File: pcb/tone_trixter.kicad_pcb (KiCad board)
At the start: 2 copper layers, 132 x 57 mm, 103 parts, among them J1 INA jack lead, J10 microSD DM3AT, J2 OUT jack lead, J3 DC 2.1mm lead, J4 Battery lead, J5 Enclosure bond, J6 OLED 1.3" 7-pin, J7 SW-L bypass, J8 INB jack lead, J9 SW-R tuner, SW1 PEC11R-4220F-S0024, U1 OPA1642AIDR, U2 OPA1642AIDR, U3 OPA1642AIDR, U4 Daisy Seed3

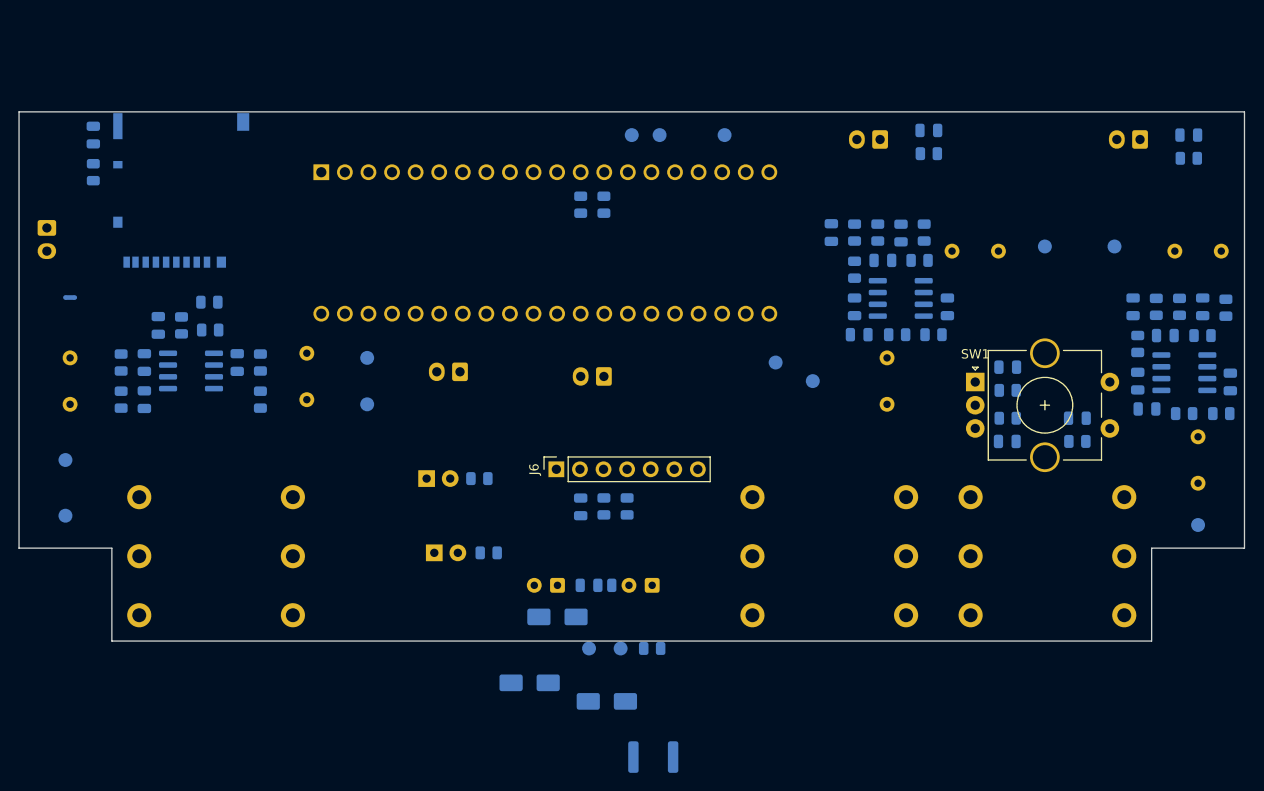
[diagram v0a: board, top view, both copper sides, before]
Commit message: pcb: output coupling caps to 1u C0G, LED/power/star placement pass
- gen_schematic: output C19/C21 10u film -> 1u C0G 1210 so they tuck
  under the OUT jack (C21->J2 tip run 3.0mm), matching the input caps
- LEDs D4/D5 forward to y=33.5 to clear the Daisy 2x20 pin field;
  silk alignment marks moved with them
- GND star (NT1) to the analog side, 6mm from the Daisy GNDA pin
- CH-B relaid under IN B (tip run 3.2mm); power section moved clear of
  the high-Z inputs (>=38mm) and out of the Daisy->USB corridor
- mirror_board_x.py: one-time X-mirror that set board handedness

Co-Authored-By: Claude Opus 4.8 <noreply@anthropic.com>
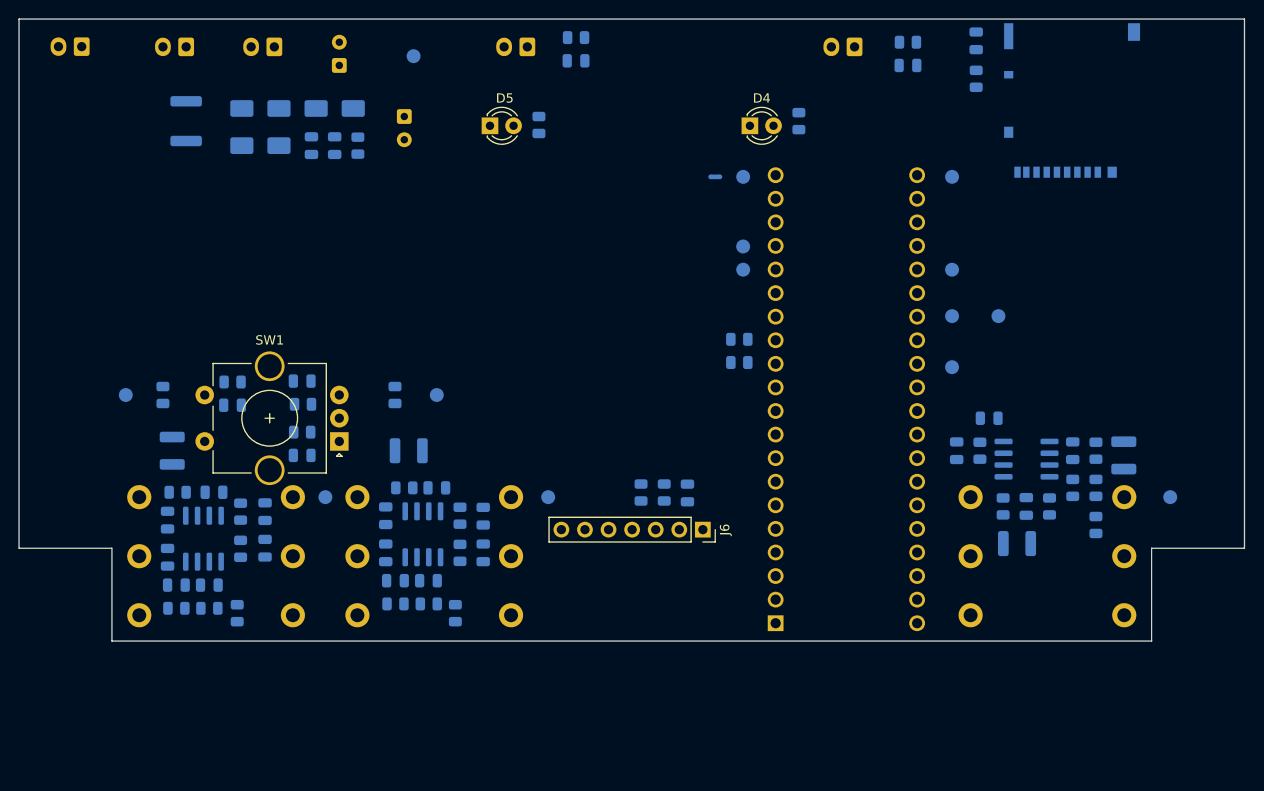
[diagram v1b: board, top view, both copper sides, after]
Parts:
- C11, C5: value 10u film -> 330n; footprint Capacitor_THT:C_Rect_L7.2mm_W7.2mm_P5.00mm_FKS2_FKP2_MKS2_MKP2 -> Capacitor_SMD:C_0805_2012Metric
- C14, C19, C21, C8: value 10u film -> 1u; footprint Capacitor_THT:C_Rect_L7.2mm_W7.2mm_P5.00mm_FKS2_FKP2_MKS2_MKP2 -> Capacitor_SMD:C_1210_3225Metric
- D4, D5: moved to F.Cu
- moved C8 115.0 mm to (46.5, 66.5), turned to 90 degrees
- moved R5 114.9 mm to (45.5, 60.5)
- moved C7 113.8 mm to (46.0, 74.0), turned to -90 degrees
- moved R8 110.4 mm to (47.0, 83.5), turned to 180 degrees
- moved C6 110.1 mm to (51.0, 71.0), turned to 0 degrees
- moved C22 110.1 mm to (46.0, 78.0), turned to 90 degrees
- moved R4 109.7 mm to (47.1, 71.0), turned to 180 degrees
- moved R6 108.2 mm to (53.5, 84.0), turned to -90 degrees
- moved TP2 107.7 mm to (41.5, 60.5), turned to 0 degrees
- moved C10 107.3 mm to (47.0, 81.0), turned to 0 degrees
- moved U1 107.2 mm to (49.9, 76.0), turned to -90 degrees
- moved R3 106.2 mm to (53.9, 73.1), turned to 90 degrees
- moved R7 104.0 mm to (50.5, 83.5), turned to 180 degrees
- moved C19 103.9 mm to (137.5, 76.5), turned to 0 degrees
- moved R2 102.7 mm to (53.9, 77.1), turned to -90 degrees
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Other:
- board size 132 x 57 mm -> 132 x 67 mm
- board text added: "D4"
- board text added: "D5"
- board text added: "DC"
- board text added: "ENC CTR"
- board text added: "J6 PIN4"
- board text added: "JACK CL"
- board text added: "USB"

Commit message: pcb: convert to 4-layer with JLC 1.6mm stackup
- 2-layer -> 4-layer: adds In1 (power plane) and In2 (ground plane).
  Inner layers sit adjacent to B, so the analog front end references
  the In2 ground plane across ~0.21mm prepreg.
- Physical stackup set to JLC standard 1.6mm 4-layer: 0.2104 prepreg /
  1.065 core / 0.2104 prepreg; 1oz outer, 0.5oz inner copper.
- Plane nets assigned at pour time: In2 = GND, In1 = power.

Co-Authored-By: Claude Opus 4.8 <noreply@anthropic.com>
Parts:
- moved TP7 5.52 mm to (136.0, 57.5)
- moved C24 0.50 mm to (134.5, 63.5)
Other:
- copper layers 2 -> 4
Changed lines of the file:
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@@
 	(layers
 		(0 "F.Cu" signal)
+		(4 "In1.Cu" power)
+		(6 "In2.Cu" power)
 		(2 "B.Cu" signal)
 		(9 "F.Adhes" user "F.Adhesive")
@@
 	)
 	(setup
+		(stackup
+			(layer "F.SilkS"
+				(type "Top Silk Screen")
+			)
+			(layer "F.Paste"
+				(type "Top Solder Paste")
+			)
+			(layer "F.Mask"
+				(type "Top Solder Mask")
+				(thickness 0.01)
+			)
+			(layer "F.Cu"
+				(type "copper")
+				(thickness 0.035)
+			)
+			(layer "dielectric 1"
+				(type "prepreg")
+				(thickness 0.2104)
+				(material "FR4")
+				(epsilon_r 4.4)
+				(loss_tangent 0.02)
+			)
+			(layer "In1.Cu"
+				(type "copper")
+				(thickness 0.0152)
+			)
+			(layer "dielectric 2"
+				(type "core")
+				(thickness 1.065)
+				(material "FR4")
+				(epsilon_r 4.6)
+				(loss_tangent 0.02)
+			)
+			(layer "In2.Cu"
+				(type "copper")
+				(thickness 0.0152)
+			)
+			(layer "dielectric 3"
+				(type "prepreg")
+				(thickness 0.2104)
+				(material "FR4")
+				(epsilon_r 4.4)
+				(loss_tangent 0.02)
+			)
+			(layer "B.Cu"
+				(type "copper")
+				(thickness 0.035)
+			)
+			(layer "B.Mask"
+				(type "Bottom Solder Mask")
+				(thickness 0.01)
+			)
+			(layer "B.Paste"
+				(type "Bottom Solder Paste")
+			)
+			(layer "B.SilkS"
+				(type "Bottom Silk Screen")
+			)
+			(copper_finish "None")
+			(dielectric_constraints no)
+		)
 		(pad_to_mask_clearance 0)
 		(allow_soldermask_bridges_in_footprints no)
@@
 	(footprint "Capacitor_SMD:C_0805_2012Metric"
 		(layer "B.Cu")
-		(at 134.5 63 180)
+		(at 134.5 63.5 180)
 		(descr "Capacitor SMD 0805 (2012 Metric), square (rectangular) end terminal, IPC-7351 nominal, (Body size source: IPC-SM-782 page 76, https://www.pcb-3d.com/wordpress/wp-content/uploads/ipc-sm-782a_amendment_1_and_2.pdf, https://docs.google.com/spreadsheets/d/1BsfQQcO9C6DZCsRaXUlFlo91Tg2WpOkGARC1WS5S8t0/edit?usp=sharing)")
 		(tags "capacitor")
 		(property "Reference" "C24"
-			(at 0 -2 0)
+			(at 0 1.5 0)
 			(layer "B.SilkS")
 			(effects
@@
 	(footprint "TestPoint:TestPoint_Pad_D1.5mm"
 		(layer "B.Cu")
-		(at 135.5 52)
+		(at 136 57.5)
 		(descr "SMD pad as test Point, diameter 1.5mm")
 		(tags "test point SMD pad")
@@
 		(tags "test point SMD pad")
 		(property "Reference" "TP9"
-			(at 0 2 180)
+			(at 2.5 0 180)
 			(layer "B.SilkS")
 			(effects
@@
 		(tags "test point SMD pad")
 		(property "Reference" "TP14"
-			(at 3 0 180)
+			(at 0 2 180)
 			(layer "B.SilkS")
 			(effects

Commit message: pcb/enclosure: OLED off-board cable-mount + template refinements
OLED moves off the board to the enclosure top face on a Dupont cable:
- J6: PinSocket_1x07 -> PinHeader_1x04 (pads GND/+3V3/SCL/SDA), re-centred
  at enc (69,67) just forward of the window, pin row along X, right-angle
  pins to point rearward; OLED_RES (D13) dropped - the 4-pin I2C module
  self-resets.
- Window set to 33x17 (black glass 34.44x18.66 minus a ~0.7mm retaining
  lip; active area 29.42x14.7 shows through). OLED modelled as top-face
  mounted; provisional header->window offset removed.

Enclosure template (fold-net work, this session):
- measured walls (front/rear 2.5, side 2.3), bottom lid 4.23; external
  outline centred on the box; front+rear fold panels; encoder shaft
  position fix; side-elevation wall thicknesses.

Regenerated 1:1 templates: mockup, side elevation, pcb top + bottom.

Co-Authored-By: Claude Opus 4.8 <noreply@anthropic.com>
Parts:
- J6: value OLED 1.3" 7-pin -> OLED I2C 1x4; footprint Connector_PinSocket_2.54mm:PinSocket_1x07_P2.54mm_Vertical -> PinHeader_1x04_P2.54mm_Vertical
- moved J6 34.9 mm to (92.2, 42.0), turned to 90 degrees
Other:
- board text added: "ENC"
- board text added: "OLED pin4"
- board text added: "OLED screen 35x20"

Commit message: pcb: flip J6 so GND is player-left, matching the OLED pin order
J6 row rotated 180 (rot 270) so GND lands on the same side as the OLED module's GND (player-left) -> the flat Dupont cable runs straight, no crossed wires. Pad holes unchanged (same 4 positions); only pin1/net order reverses.

Co-Authored-By: Claude Opus 4.8 <noreply@anthropic.com>
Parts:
- moved J6 7.62 mm to (99.8, 42.0), turned to -90 degrees
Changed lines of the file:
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@@
 	(footprint "PinHeader_1x04_P2.54mm_Vertical"
 		(layer "F.Cu")
-		(at 92.19 42 90)
+		(at 99.81 42 -90)
 		(descr "Through hole straight pin header, 1x04, 2.54mm pitch, single row")
 		(tags "Through hole pin header THT 1x04 2.54mm single row")
 		(property "Reference" "J6"
-			(at 0 -2.38 90)
+			(at 0 -2.38 270)
 			(layer "F.SilkS")
 			(effects
@@
 		)
 		(property "Value" "OLED I2C 1x4"
-			(at 0 10 90)
+			(at 0 10 270)
 			(layer "F.Fab")
 			(effects
@@
 		)
 		(property "Datasheet" ""
-			(at 0 0 90)
+			(at 0 0 270)
 			(layer "F.Fab")
 			(hide yes)
@@
 		)
 		(property "Description" ""
-			(at 0 0 90)
+			(at 0 0 270)
 			(layer "F.Fab")
 			(hide yes)
@@
 		)
 		(property "KiLib_Generator" "connector/pin_header_socket"
-			(at 0 0 90)
+			(at 0 0 270)
 			(layer "F.SilkS")
 			(hide yes)
@@
 		(duplicate_pad_numbers_are_jumpers no)
 		(fp_line
+			(start -1.38 9)
+			(end 1.38 9)
+			(stroke
+				(width 0.12)
+				(type solid)
+			)
+			(layer "F.SilkS")
+		)
+		(fp_line
+			(start -1.38 1.27)
+			(end -1.38 9)
+			(stroke
+				(width 0.12)
+				(type solid)
+			)
+			(layer "F.SilkS")
+		)
+		(fp_line
+			(start -1.38 1.27)
+			(end 1.38 1.27)
+			(stroke
+				(width 0.12)
+				(type solid)
+			)
+			(layer "F.SilkS")
+		)
+		(fp_line
+			(start 1.38 1.27)
+			(end 1.38 9)
+			(stroke
+				(width 0.12)
+				(type solid)
+			)
+			(layer "F.SilkS")
+		)
+		(fp_line
+			(start -1.38 0)
+			(end -1.38 -1.38)
+			(stroke
+				(width 0.12)
+				(type solid)
+			)
+			(layer "F.SilkS")
+		)
+		(fp_line
 			(start -1.38 -1.38)
 			(end 0 -1.38)
-			(stroke
-				(width 0.12)
-				(type solid)
-			)
-			(layer "F.SilkS")
-		)
-		(fp_line
-			(start -1.38 0)
-			(end -1.38 -1.38)
-			(stroke
-				(width 0.12)
-				(type solid)
-			)
-			(layer "F.SilkS")
-		)
-		(fp_line
-			(start 1.38 1.27)
-			(end 1.38 9)
-			(stroke
-				(width 0.12)
-				(type solid)
-			)
-			(layer "F.SilkS")
-		)
-		(fp_line
-			(start -1.38 1.27)
-			(end 1.38 1.27)
-			(stroke
-				(width 0.12)
-				(type solid)
-			)
-			(layer "F.SilkS")
-		)
-		(fp_line
-			(start -1.38 1.27)
-			(end -1.38 9)
-			(stroke
-				(width 0.12)
-				(type solid)
-			)
-			(layer "F.SilkS")
-		)
-		(fp_line
-			(start -1.38 9)
-			(end 1.38 9)
 			(stroke
 				(width 0.12)
@@
 		)
 		(fp_line
+			(start -1.27 8.89)
+			(end -1.27 -0.635)
+			(stroke
+				(width 0.1)
+				(type solid)
+			)
+			(layer "F.Fab")
+		)
+		(fp_line
+			(start 1.27 8.89)
+			(end -1.27 8.89)
+			(stroke
+				(width 0.1)
+				(type solid)
+			)
+			(layer "F.Fab")
+		)
+		(fp_line
+			(start -1.27 -0.635)
+			(end -0.635 -1.27)
+			(stroke
+				(width 0.1)
+				(type solid)
+			)
+			(layer "F.Fab")
+		)
+		(fp_line
+			(start -0.635 -1.27)
+			(end 1.27 -1.27)
+			(stroke
+				(width 0.1)
+				(type solid)
+			)
+			(layer "F.Fab")
+		)
+		(fp_line
 			(start 1.27 -1.27)
 			(end 1.27 8.89)
@@
 			(layer "F.Fab")
 		)
-		(fp_line
-			(start -0.635 -1.27)
-			(end 1.27 -1.27)
-			(stroke
-				(width 0.1)
-				(type solid)
-			)
-			(layer "F.Fab")
-		)
-		(fp_line
-			(start -1.27 -0.635)
-			(end -0.635 -1.27)
-			(stroke
-				(width 0.1)
-				(type solid)
-			)
-			(layer "F.Fab")
-		)
-		(fp_line
-			(start 1.27 8.89)
-			(end -1.27 8.89)
-			(stroke
-				(width 0.1)
-				(type solid)
-			)
-			(layer "F.Fab")
-		)
-		(fp_line
-			(start -1.27 8.89)
-			(end -1.27 -0.635)
-			(stroke
-				(width 0.1)
-				(type solid)
-			)
-			(layer "F.Fab")
-		)
 		(fp_text user "${REFERENCE}"
-			(at 0 3.81 180)
+			(at 0 3.81 0)
 			(layer "F.Fab")
 			(effects
@@
 		)
 		(pad "1" thru_hole rect
-			(at 0 0 90)
+			(at 0 0 270)
 			(size 1.7 1.7)
 			(drill 1)
@@
 		)
 		(pad "2" thru_hole circle
-			(at 0 2.54 90)
+			(at 0 2.54 270)
 			(size 1.7 1.7)
 			(drill 1)
@@
 		)
 		(pad "3" thru_hole circle
-			(at 0 5.08 90)
+			(at 0 5.08 270)
 			(size 1.7 1.7)
 			(drill 1)
@@
 		)
 		(pad "4" thru_hole circle
-			(at 0 7.62 90)
-			(size 1.7 1.7)
-			(drill 1)
+			(at 0 7.62 270)
+			(size 1.7 1.7)
+			(drill 1)

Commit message: pcb: J6 right-angle footprint; drop stale OLED pin4 silk; add OLED screen ghost
- J6 -> PinHeader_1x04_Horizontal (right-angle), rot 270: GND player-left, mating pins toward the rear (toward the OLED) so the flat Dupont cable runs straight. Same 4 holes/nets, GND/3V3/SCL/SDA.

- Deleted stale 'OLED pin4' (F.Silk), 'J6 PIN4' (B.Silk) and 'OLED screen 35x20' (User.Drawings) markers from the old board-mounted layout.

- Added OLED screen ghost on Dwgs.User at enc (69,88): module outline 36x34 (keep-clear) + screen window 33x17 + label, visible on the pcb-top print.

Co-Authored-By: Claude Opus 4.8 <noreply@anthropic.com>
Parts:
- J6: value OLED I2C 1x4 -> OLED I2C 1x4 (right-angle); footprint PinHeader_1x04_P2.54mm_Vertical -> PinHeader_1x04_P2.54mm_Horizontal
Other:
- board text added: "OLED screen 33x17 (top-face ghost)"
- board text removed: "J6 PIN4"
- board text removed: "OLED pin4"
- board text removed: "OLED screen 35x20"
